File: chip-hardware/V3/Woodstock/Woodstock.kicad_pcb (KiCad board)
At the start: 2 copper layers, 22.8 x 20.8 mm, 11 parts, among them J1 501461-0491, U1 MCP9808_MSOP, U2 LIS3DH

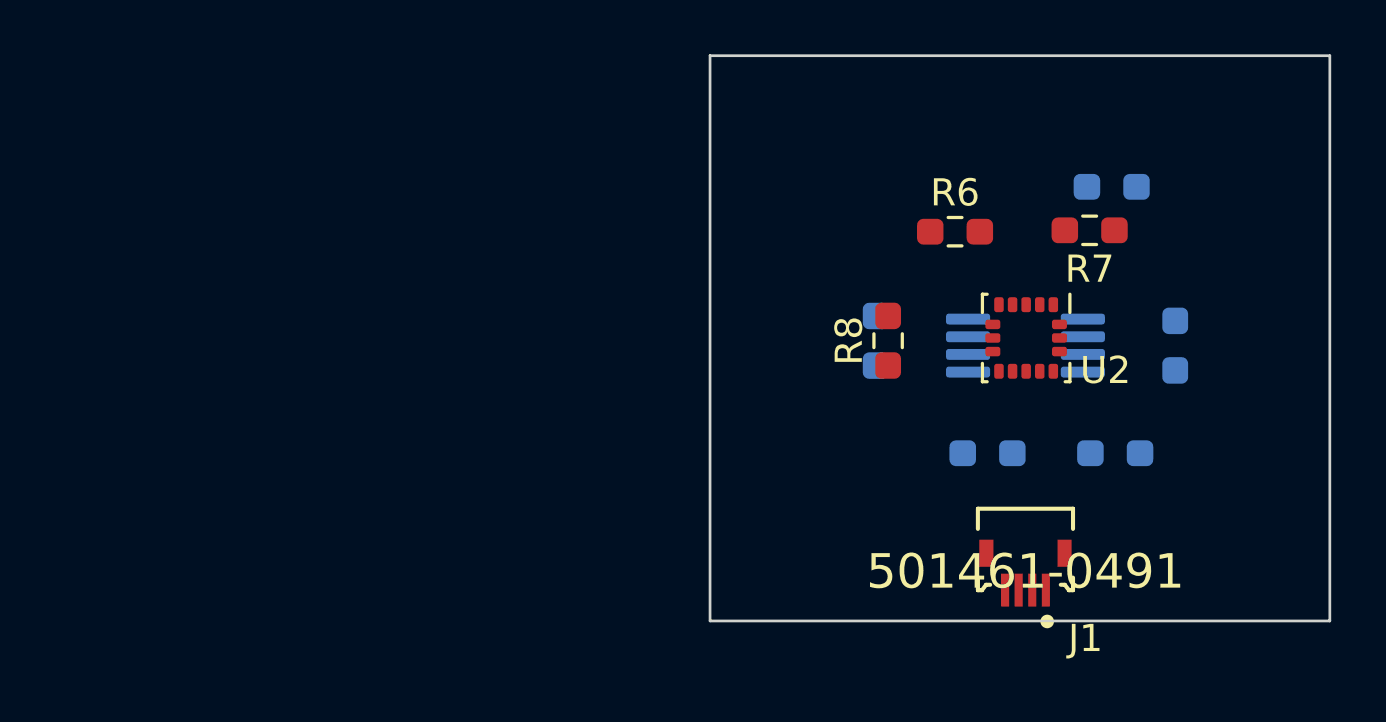
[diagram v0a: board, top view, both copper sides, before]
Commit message: edge cuts introduced
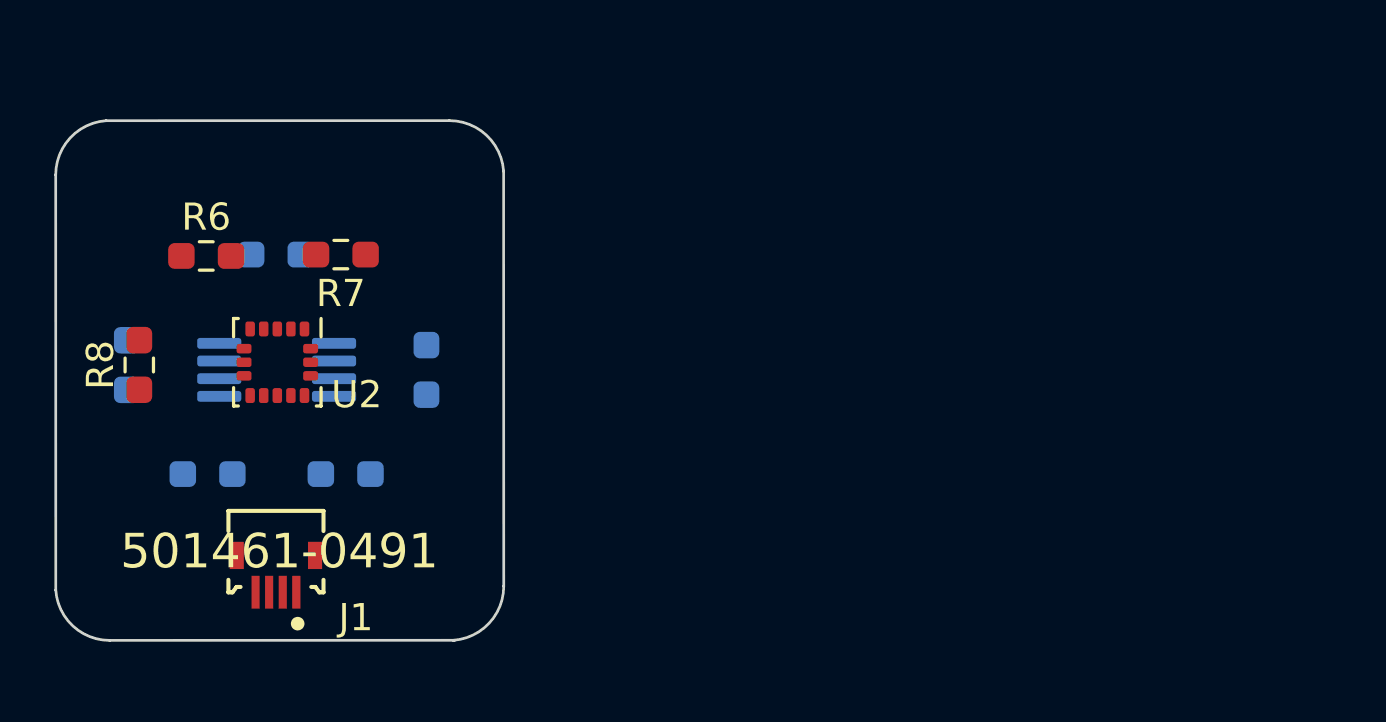
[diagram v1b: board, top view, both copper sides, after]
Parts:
- moved R3 30.9 mm to (151.0, 92.2)
- moved R5 28.7 mm to (148.5, 100.3)
- moved R4 28.3 mm to (153.6, 100.3)
- moved J1 27.6 mm to (151.0, 104.0)
- moved R2 27.6 mm to (145.5, 96.3)
- moved R8 27.6 mm to (146.0, 96.3)
- moved R1 27.6 mm to (156.5, 96.5)
- moved R6 27.6 mm to (148.4, 92.3)
- moved R7 27.6 mm to (153.4, 92.2)
- moved U1 27.6 mm to (151.0, 96.5)
- moved U2 27.6 mm to (151.1, 96.2)
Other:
- board size 22.8 x 20.8 mm -> 16.5 x 19.1 mm
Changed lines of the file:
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@@
   (net 17 "unconnected-(U2-Pad16)")
   (footprint "Resistor_SMD:R_0603_1608Metric_Pad0.98x0.95mm_HandSolder" (layer "F.Cu")
-    (at 173.5328 95.4005 90)
+    (at 145.97436 96.29336 90)
     (descr "Resistor SMD 0603 (1608 Metric), square (rectangular) end terminal, IPC_7351 nominal with elongated pad for handsoldering. (Body size source: IPC-SM-782 page 72, https://www.pcb-3d.com/wordpress/wp-content/uploads/ipc-sm-782a_amendment_1_and_2.pdf), generated with kicad-footprint-generator")
     (tags "resistor handsolder")
@@
   )
   (footprint "5014610491:Molex-501461-0491-Manufacturer_Recommended" (layer "F.Cu")
-    (at 178.5874 103.9011 180)
+    (at 151.00356 103.98116 180)
     (property "Circuits Loaded" "4")
     (property "Component Link 1 Description" "Manufacturer URL")
@@
     (property "vault revision" "5F166C2B-E9D9-4135-9ADB-F1D93D2D935E")
     (attr through_hole)
-    (fp_text reference "J1" (at -2.849999 -2.457502) (layer "F.SilkS")
+    (fp_text reference "J1" (at -3.5814 -1.6105) (layer "F.SilkS")
       (effects (font (size 1 1) (thickness 0.15)) (justify right))
     )
-    (fp_text value "501461-0491" (at 0 0) (layer "F.SilkS")
+    (fp_text value "501461-0491" (at -0.127 0.8279 180) (layer "F.SilkS")
       (effects (font (size 1.27 1.27) (thickness 0.15)))
     )
@@
   )
   (footprint "Package_LGA:LGA-16_3x3mm_P0.5mm_LayoutBorder3x5y" (layer "F.Cu")
-    (at 178.6128 95.3008 -90)
+    (at 151.05436 96.19366 -90)
     (descr "LGA, 16 Pin (http://www.st.com/resource/en/datasheet/lis331hh.pdf), generated with kicad-footprint-generator ipc_noLead_generator.py")
     (tags "LGA NoLead")
@@
   )
   (footprint "Resistor_SMD:R_0603_1608Metric_Pad0.98x0.95mm_HandSolder" (layer "F.Cu")
-    (at 180.9496 91.3384 180)
+    (at 153.39116 92.23126 180)
     (descr "Resistor SMD 0603 (1608 Metric), square (rectangular) end terminal, IPC_7351 nominal with elongated pad for handsoldering. (Body size source: IPC-SM-782 page 72, https://www.pcb-3d.com/wordpress/wp-content/uploads/ipc-sm-782a_amendment_1_and_2.pdf), generated with kicad-footprint-generator")
     (tags "resistor handsolder")
@@
   )
   (footprint "Resistor_SMD:R_0603_1608Metric_Pad0.98x0.95mm_HandSolder" (layer "F.Cu")
-    (at 175.9966 91.3892)
+    (at 148.43816 92.28206)
     (descr "Resistor SMD 0603 (1608 Metric), square (rectangular) end terminal, IPC_7351 nominal with elongated pad for handsoldering. (Body size source: IPC-SM-782 page 72, https://www.pcb-3d.com/wordpress/wp-content/uploads/ipc-sm-782a_amendment_1_and_2.pdf), generated with kicad-footprint-generator")
     (tags "resistor handsolder")
@@
   )
   (footprint "Package_SO:MSOP-8_3x3mm_P0.65mm" (layer "B.Cu")
-    (at 178.5874 95.5802 180)
+    (at 151.02896 96.47306 180)
     (descr "MSOP, 8 Pin (https://www.jedec.org/system/files/docs/mo-187F.pdf variant AA), generated with kicad-footprint-generator ipc_gullwing_generator.py")
     (tags "MSOP SO")
@@
   )
   (footprint "Resistor_SMD:R_0603_1608Metric_Pad0.98x0.95mm_HandSolder" (layer "B.Cu")
-    (at 181.7624 89.7382 180)
+    (at 151.00356 92.23126 180)
     (descr "Resistor SMD 0603 (1608 Metric), square (rectangular) end terminal, IPC_7351 nominal with elongated pad for handsoldering. (Body size source: IPC-SM-782 page 72, https://www.pcb-3d.com/wordpress/wp-content/uploads/ipc-sm-782a_amendment_1_and_2.pdf), generated with kicad-footprint-generator")
     (tags "resistor handsolder")
@@
   )
   (footprint "Resistor_SMD:R_0603_1608Metric_Pad0.98x0.95mm_HandSolder" (layer "B.Cu")
-    (at 177.1923 99.5426)
+    (at 148.48896 100.30846)
     (descr "Resistor SMD 0603 (1608 Metric), square (rectangular) end terminal, IPC_7351 nominal with elongated pad for handsoldering. (Body size source: IPC-SM-782 page 72, https://www.pcb-3d.com/wordpress/wp-content/uploads/ipc-sm-782a_amendment_1_and_2.pdf), generated with kicad-footprint-generator")
     (tags "resistor handsolder")
@@
   )
   (footprint "Resistor_SMD:R_0603_1608Metric_Pad0.98x0.95mm_HandSolder" (layer "B.Cu")
-    (at 173.0756 95.4043 -90)
+    (at 145.51716 96.29716 -90)
     (descr "Resistor SMD 0603 (1608 Metric), square (rectangular) end terminal, IPC_7351 nominal with elongated pad for handsoldering. (Body size source: IPC-SM-782 page 72, https://www.pcb-3d.com/wordpress/wp-content/uploads/ipc-sm-782a_amendment_1_and_2.pdf), generated with kicad-footprint-generator")
     (tags "resistor handsolder")
@@
   )
   (footprint "Resistor_SMD:R_0603_1608Metric_Pad0.98x0.95mm_HandSolder" (layer "B.Cu")
-    (at 184.0992 95.5821 90)
+    (at 156.54076 96.47496 90)
     (descr "Resistor SMD 0603 (1608 Metric), square (rectangular) end terminal, IPC_7351 nominal with elongated pad for handsoldering. (Body size source: IPC-SM-782 page 72, https://www.pcb-3d.com/wordpress/wp-content/uploads/ipc-sm-782a_amendment_1_and_2.pdf), generated with kicad-footprint-generator")
     (tags "resistor handsolder")
@@
   )
   (footprint "Resistor_SMD:R_0603_1608Metric_Pad0.98x0.95mm_HandSolder" (layer "B.Cu")
-    (at 181.8913 99.5426 180)
+    (at 153.56896 100.30846 180)
     (descr "Resistor SMD 0603 (1608 Metric), square (rectangular) end terminal, IPC_7351 nominal with elongated pad for handsoldering. (Body size source: IPC-SM-782 page 72, https://www.pcb-3d.com/wordpress/wp-content/uploads/ipc-sm-782a_amendment_1_and_2.pdf), generated with kicad-footprint-generator")
     (tags "resistor handsolder")
@@
     )
   )
-  (gr_rect (start 166.9796 84.9122) (end 189.7888 105.7148) (layer "Edge.Cuts") (width 0.1) (fill none))
+  (gr_line (start 157.389938 87.301761) (end 144.752701 87.30366) (layer "Edge.Cuts") (width 0.1))
+  (gr_arc (start 144.88216 106.42986) (mid 143.525398 105.894001) (end 142.90096 104.57566) (layer "Edge.Cuts") (width 0.1))
+  (gr_line (start 142.90096 104.57566) (end 142.898501 89.295422) (layer "Edge.Cuts") (width 0.1))
+  (gr_line (start 144.88216 106.42986) (end 157.58216 106.426) (layer "Edge.Cuts") (width 0.1))
+  (gr_arc (start 157.389938 87.301761) (mid 158.75056 87.83706) (end 159.3817 89.155961) (layer "Edge.Cuts") (width 0.1))
+  (gr_line (start 159.387459 104.434238) (end 159.3817 89.155961) (layer "Edge.Cuts") (width 0.1))
+  (gr_arc (start 142.898501 89.295422) (mid 143.4338 87.9348) (end 144.752701 87.30366) (layer "Edge.Cuts") (width 0.1))
+  (gr_arc (start 159.387459 104.434238) (mid 158.85216 105.79486) (end 157.533259 106.426) (layer "Edge.Cuts") (width 0.1))
 )

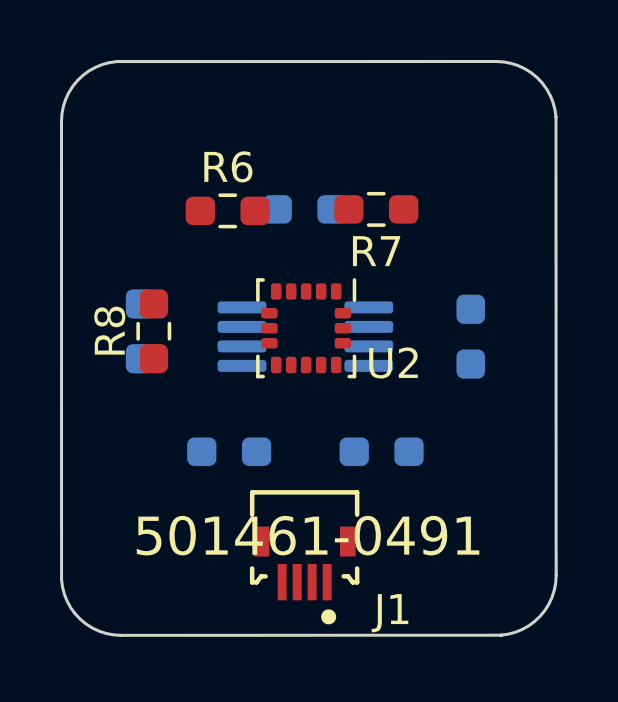
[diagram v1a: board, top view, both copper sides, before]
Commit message: Front traces added onto board
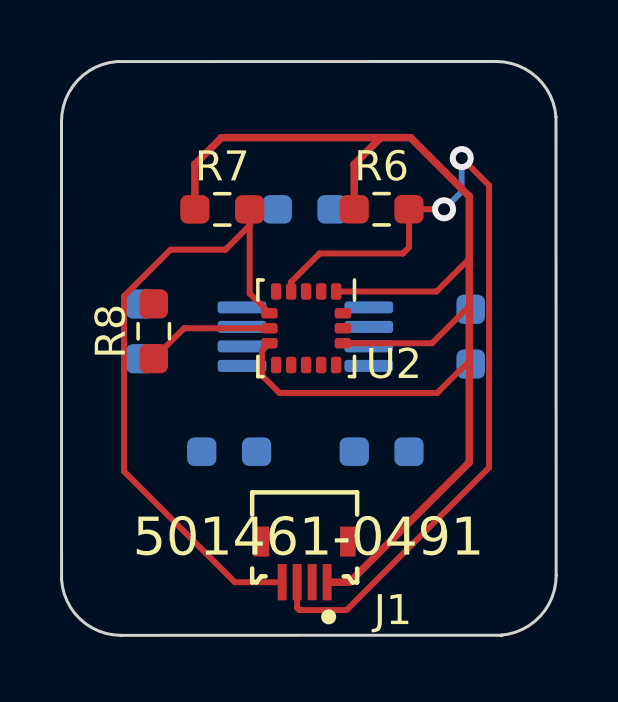
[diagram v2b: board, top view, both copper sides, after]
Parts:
- moved R7 5.13 mm to (148.3, 92.2), turned to 0 degrees
- moved R6 5.13 mm to (153.6, 92.2)
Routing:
- net +3V3: track 0.00 -> 48.2 mm
- net /SCL: track 0.00 -> 29.1 mm, vias 0 -> 2
- net /SDA: track 0.00 -> 22.1 mm
- net Net-(R8-Pad1): track 0.00 -> 4.27 mm
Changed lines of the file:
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@@
   )
   (setup
+    (stackup
+      (layer "F.SilkS" (type "Top Silk Screen"))
+      (layer "F.Paste" (type "Top Solder Paste"))
+      (layer "F.Mask" (type "Top Solder Mask") (thickness 0.01))
+      (layer "F.Cu" (type "copper") (thickness 0.035))
+      (layer "dielectric 1" (type "core") (thickness 1.51) (material "FR4") (epsilon_r 4.5) (loss_tangent 0.02))
+      (layer "B.Cu" (type "copper") (thickness 0.035))
+      (layer "B.Mask" (type "Bottom Solder Mask") (thickness 0.01))
+      (layer "B.Paste" (type "Bottom Solder Paste"))
+      (layer "B.SilkS" (type "Bottom Silk Screen"))
+      (copper_finish "None")
+      (dielectric_constraints no)
+    )
     (pad_to_mask_clearance 0)
     (pcbplotparams
@@
   )
   (footprint "Resistor_SMD:R_0603_1608Metric_Pad0.98x0.95mm_HandSolder" (layer "F.Cu")
-    (at 153.39116 92.23126 180)
+    (at 148.2579 92.23126)
     (descr "Resistor SMD 0603 (1608 Metric), square (rectangular) end terminal, IPC_7351 nominal with elongated pad for handsoldering. (Body size source: IPC-SM-782 page 72, https://www.pcb-3d.com/wordpress/wp-content/uploads/ipc-sm-782a_amendment_1_and_2.pdf), generated with kicad-footprint-generator")
     (tags "resistor handsolder")
@@
     (fp_line (start -0.8 0.4125) (end -0.8 -0.4125) (layer "F.Fab") (width 0.1))
     (fp_line (start 0.8 0.4125) (end -0.8 0.4125) (layer "F.Fab") (width 0.1))
-    (pad "1" smd roundrect (at -0.9125 0 180) (size 0.975 0.95) (layers "F.Cu" "F.Paste" "F.Mask") (roundrect_rratio 0.25)
+    (pad "1" smd roundrect (at -0.9125 0) (size 0.975 0.95) (layers "F.Cu" "F.Paste" "F.Mask") (roundrect_rratio 0.25)
       (net 6 "+3V3") (pintype "passive"))
-    (pad "2" smd roundrect (at 0.9125 0 180) (size 0.975 0.95) (layers "F.Cu" "F.Paste" "F.Mask") (roundrect_rratio 0.25)
+    (pad "2" smd roundrect (at 0.9125 0) (size 0.975 0.95) (layers "F.Cu" "F.Paste" "F.Mask") (roundrect_rratio 0.25)
       (net 3 "/SDA") (pintype "passive"))
     (model "${KICAD6_3DMODEL_DIR}/Resistor_SMD.3dshapes/R_0603_1608Metric.wrl"
@@
   )
   (footprint "Resistor_SMD:R_0603_1608Metric_Pad0.98x0.95mm_HandSolder" (layer "F.Cu")
-    (at 148.43816 92.28206)
+    (at 153.5684 92.2274)
     (descr "Resistor SMD 0603 (1608 Metric), square (rectangular) end terminal, IPC_7351 nominal with elongated pad for handsoldering. (Body size source: IPC-SM-782 page 72, https://www.pcb-3d.com/wordpress/wp-content/uploads/ipc-sm-782a_amendment_1_and_2.pdf), generated with kicad-footprint-generator")
     (tags "resistor handsolder")
@@
   (gr_arc (start 142.898501 89.295422) (mid 143.4338 87.9348) (end 144.752701 87.30366) (layer "Edge.Cuts") (width 0.1))
   (gr_arc (start 159.387459 104.434238) (mid 158.85216 105.79486) (end 157.533259 106.426) (layer "Edge.Cuts") (width 0.1))
+  (segment (start 149.1704 95.0347) (end 149.1704 92.23126) (width 0.2) (layer "F.Cu") (net 3))
+  (segment (start 144.9832 95.12506) (end 146.53466 93.5736) (width 0.2) (layer "F.Cu") (net 3))
+  (segment (start 148.676862 104.658662) (end 144.9832 100.965) (width 0.2) (layer "F.Cu") (net 3))
+  (segment (start 144.9832 100.965) (end 144.9832 95.12506) (width 0.2) (layer "F.Cu") (net 3))
+  (segment (start 149.82936 95.69366) (end 149.1704 95.0347) (width 0.2) (layer "F.Cu") (net 3))
+  (segment (start 150.253559 104.658662) (end 148.676862 104.658662) (width 0.2) (layer "F.Cu") (net 3))
+  (segment (start 148.3614 93.5736) (end 149.1704 92.7646) (width 0.2) (layer "F.Cu") (net 3))
+  (segment (start 146.53466 93.5736) (end 148.3614 93.5736) (width 0.2) (layer "F.Cu") (net 3))
+  (segment (start 149.1704 92.7646) (end 149.1704 92.23126) (width 0.2) (layer "F.Cu") (net 3))
+  (segment (start 151.500092 93.7006) (end 154.2796 93.7006) (width 0.2) (layer "F.Cu") (net 4))
+  (segment (start 154.2796 93.7006) (end 154.4809 93.4993) (width 0.2) (layer "F.Cu") (net 4))
+  (segment (start 150.753558 105.512682) (end 150.828676 105.5878) (width 0.2) (layer "F.Cu") (net 4))
+  (segment (start 157.1498 91.431402) (end 156.239699 90.521301) (width 0.2) (layer "F.Cu") (net 4))
+  (segment (start 150.55436 94.646332) (end 151.500092 93.7006) (width 0.2) (layer "F.Cu") (net 4))
+  (segment (start 152.4 105.5878) (end 157.1498 100.838) (width 0.2) (layer "F.Cu") (net 4))
+  (segment (start 150.828676 105.5878) (end 152.4 105.5878) (width 0.2) (layer "F.Cu") (net 4))
+  (segment (start 155.6512 92.2274) (end 154.4809 92.2274) (width 0.2) (layer "F.Cu") (net 4))
+  (segment (start 150.753558 104.658662) (end 150.753558 105.512682) (width 0.2) (layer "F.Cu") (net 4))
+  (segment (start 157.1498 91.8718) (end 157.1498 91.431402) (width 0.2) (layer "F.Cu") (net 4))
+  (segment (start 154.4809 93.4993) (end 154.4809 92.2274) (width 0.2) (layer "F.Cu") (net 4))
+  (segment (start 157.1498 100.838) (end 157.1498 91.8718) (width 0.2) (layer "F.Cu") (net 4))
+  (segment (start 150.55436 94.96866) (end 150.55436 94.646332) (width 0.2) (layer "F.Cu") (net 4))
+  (via (at 156.239699 90.521301) (size 0.8) (drill 0.4) (layers "F.Cu" "B.Cu") (net 4))
+  (via (at 155.6512 92.2274) (size 0.8) (drill 0.4) (layers "F.Cu" "B.Cu") (net 4))
+  (segment (start 156.239699 91.638901) (end 155.6512 92.2274) (width 0.2) (layer "B.Cu") (net 4))
+  (segment (start 156.239699 90.521301) (end 156.239699 91.638901) (width 0.2) (layer "B.Cu") (net 4))
+  (segment (start 156.4894 95.4532) (end 156.4894 93.8784) (width 0.25) (layer "F.Cu") (net 6))
+  (segment (start 149.57984 97.766468) (end 150.162172 98.3488) (width 0.2) (layer "F.Cu") (net 6))
+  (segment (start 152.27936 96.69366) (end 155.24894 96.69366) (width 0.2) (layer "F.Cu") (net 6))
+  (segment (start 152.497577 104.658662) (end 156.4894 100.666839) (width 0.25) (layer "F.Cu") (net 6))
+  (segment (start 147.3454 90.7288) (end 147.3454 92.23126) (width 0.25) (layer "F.Cu") (net 6))
+  (segment (start 152.05436 94.96866) (end 155.39914 94.96866) (width 0.2) (layer "F.Cu") (net 6))
+  (segment (start 153.543 89.8398) (end 148.2344 89.8398) (width 0.25) (layer "F.Cu") (net 6))
+  (segment (start 149.82936 96.69366) (end 149.57984 96.94318) (width 0.2) (layer "F.Cu") (net 6))
+  (segment (start 156.4894 91.7956) (end 154.5336 89.8398) (width 0.25) (layer "F.Cu") (net 6))
+  (segment (start 150.162172 98.3488) (end 155.4226 98.3488) (width 0.2) (layer "F.Cu") (net 6))
+  (segment (start 155.24894 96.69366) (end 156.4894 95.4532) (width 0.2) (layer "F.Cu") (net 6))
+  (segment (start 154.5336 89.8398) (end 153.543 89.8398) (width 0.25) (layer "F.Cu") (net 6))
+  (segment (start 156.4894 93.8784) (end 156.4894 91.7956) (width 0.25) (layer "F.Cu") (net 6))
+  (segment (start 155.39914 94.96866) (end 156.4894 93.8784) (width 0.2) (layer "F.Cu") (net 6))
+  (segment (start 151.753559 104.658662) (end 152.497577 104.658662) (width 0.25) (layer "F.Cu") (net 6))
+  (segment (start 156.4894 97.282) (end 156.4894 95.4532) (width 0.25) (layer "F.Cu") (net 6))
+  (segment (start 152.6559 90.7269) (end 152.6559 92.2274) (width 0.25) (layer "F.Cu") (net 6))
+  (segment (start 153.543 89.8398) (end 152.6559 90.7269) (width 0.25) (layer "F.Cu") (net 6))
+  (segment (start 155.4226 98.3488) (end 156.4894 97.282) (width 0.2) (layer "F.Cu") (net 6))
+  (segment (start 148.2344 89.8398) (end 147.3454 90.7288) (width 0.25) (layer "F.Cu") (net 6))
+  (segment (start 149.57984 96.94318) (end 149.57984 97.766468) (width 0.2) (layer "F.Cu") (net 6))
+  (segment (start 156.4894 100.666839) (end 156.4894 97.282) (width 0.25) (layer "F.Cu") (net 6))
+  (segment (start 145.97436 97.20586) (end 146.98656 96.19366) (width 0.2) (layer "F.Cu") (net 9))
+  (segment (start 146.98656 96.19366) (end 149.82936 96.19366) (width 0.2) (layer "F.Cu") (net 9))
 )
